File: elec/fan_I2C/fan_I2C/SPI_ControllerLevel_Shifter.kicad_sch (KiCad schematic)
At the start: 32 parts, among them J301 RJ12_6P6C_HORZ, J302 0.100_2Pin, Q301 BSS138, Q302 BSS138, Q303 BSS138, Q304 BSS138

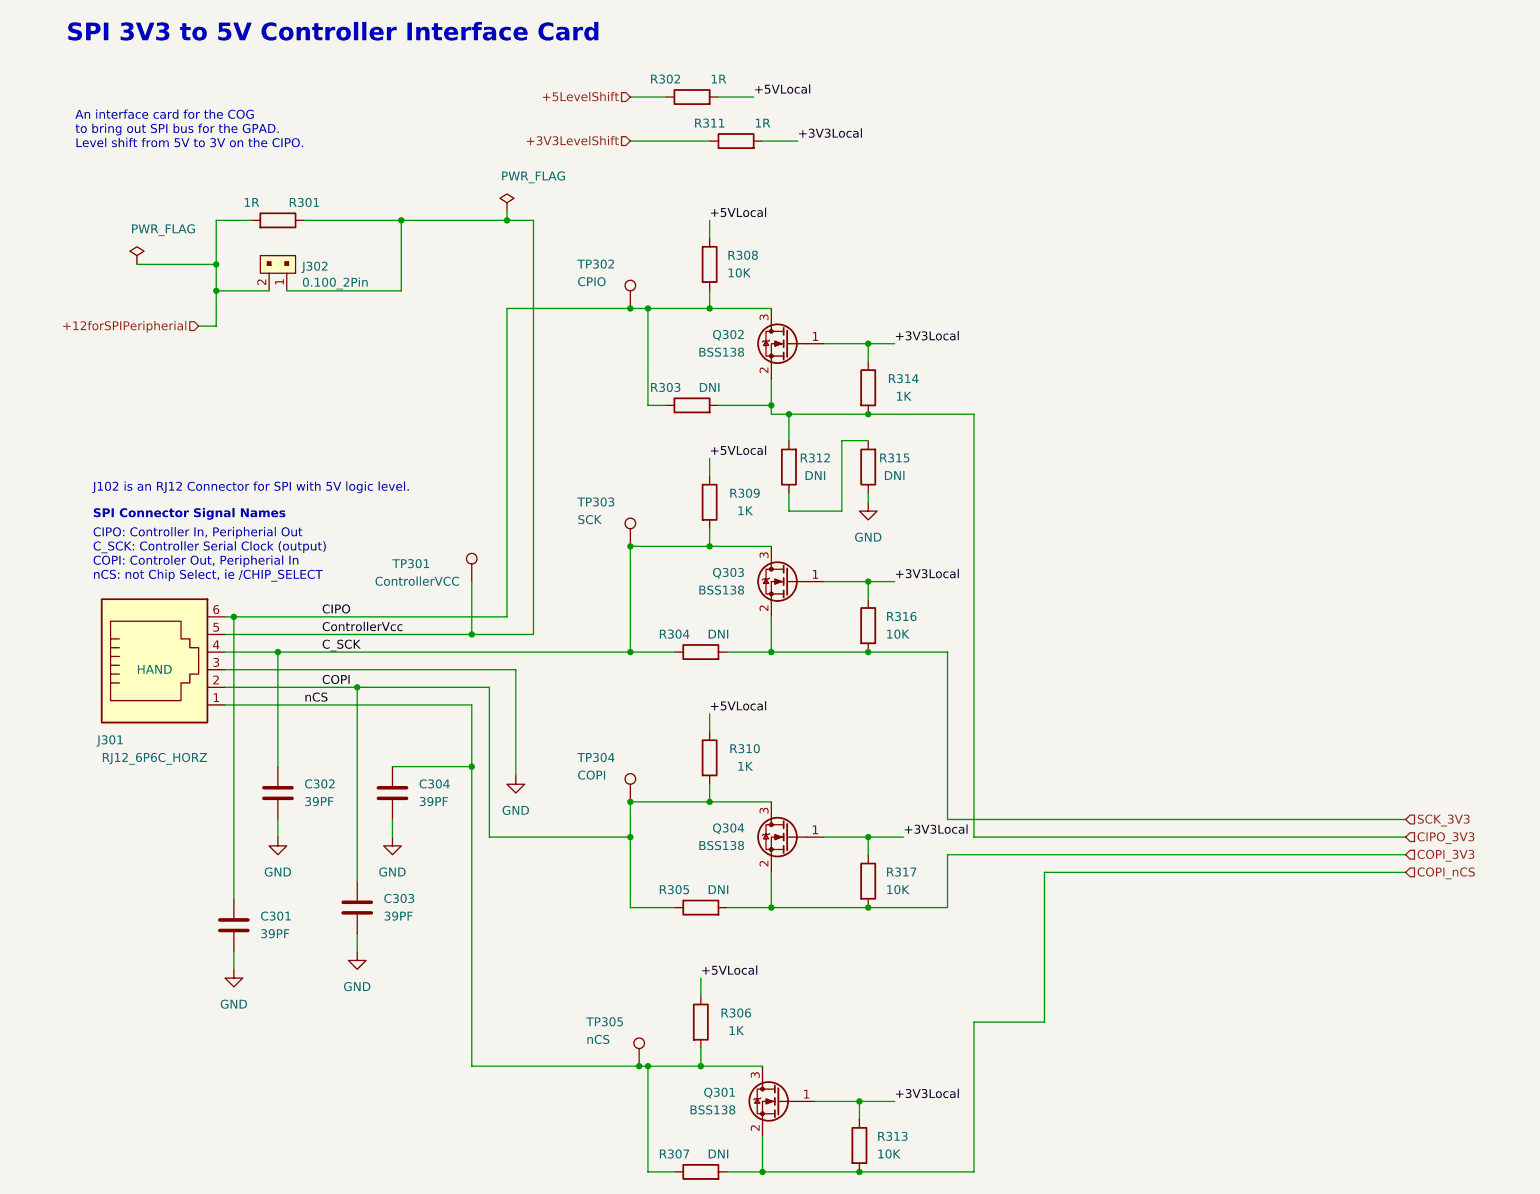
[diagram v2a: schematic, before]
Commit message: Add Connectors like Roberts Fritzing.
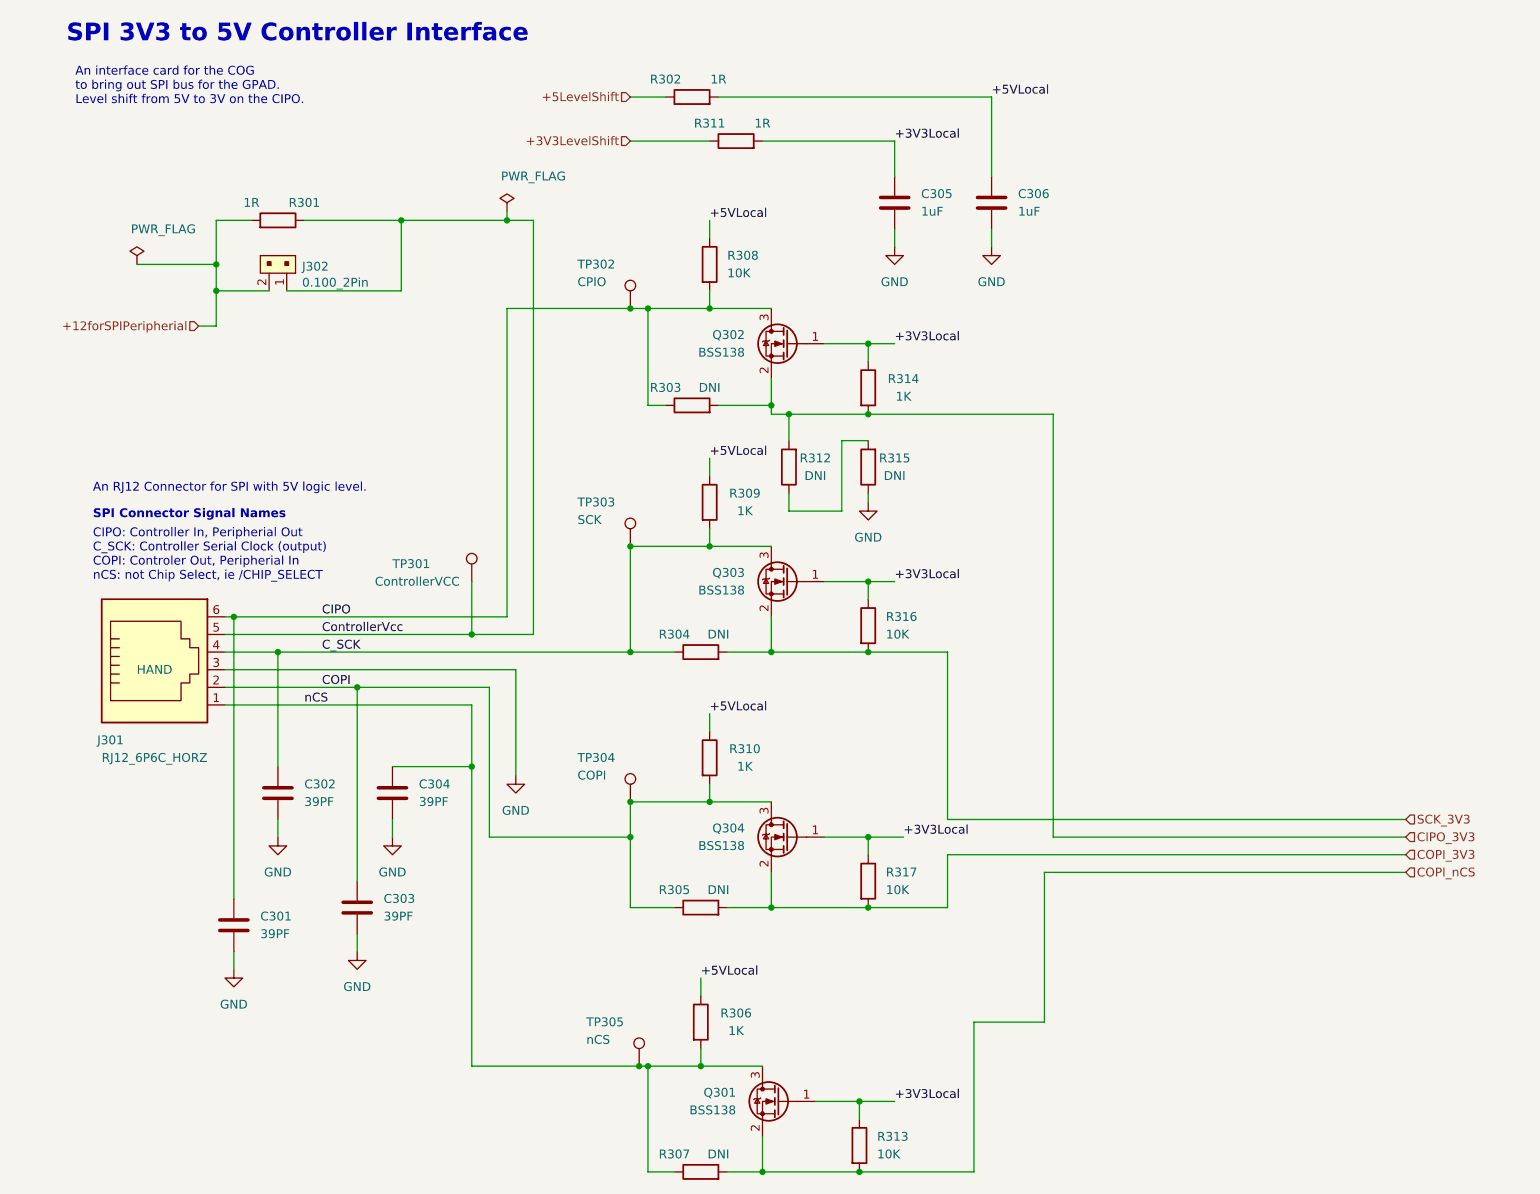
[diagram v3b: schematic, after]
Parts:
- added C305, C306: 1uF, Capacitor_SMD:C_0603_1608Metric_Pad1.08x0.95mm_HandSolder, symbol Device:C
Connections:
- net +3V3Local: now also C305.1
- net +5VLocal: now also C306.1
- net GND: now also C305.2, C306.2
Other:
- note added: "An RJ12 Connector for SPI with 5V logic level."
- note added: "SPI 3V3 to 5V Controller Interface"
- note removed: "J102 is an RJ12 Connector for SPI with 5V logic level."
- note removed: "SPI 3V3 to 5V Controller Interface Card"
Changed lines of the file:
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@@
+    (stroke (width 0) (type default) (color 0 0 0 0))
+  )
+  (wire (pts (xy 149.86 44.45) (xy 149.86 46.99))
     (stroke (width 0) (type default) (color 0 0 0 0))
   )
@@
     (stroke (width 0) (type default) (color 0 0 0 0))
   )
-  (wire (pts (xy 132.08 71.12) (xy 147.32 71.12))
+  (wire (pts (xy 132.08 71.12) (xy 158.75 71.12))
     (stroke (width 0) (type default) (color 0 0 0 0))
   )
@@
     (stroke (width 0) (type default) (color 0 0 0 0))
   )
+  (wire (pts (xy 135.89 44.45) (xy 135.89 46.99))
+    (stroke (width 0) (type default) (color 0 0 0 0))
+  )
   (wire (pts (xy 109.22 127) (xy 118.11 127))
     (stroke (width 0) (type default) (color 0 0 0 0))
@@
     (stroke (width 0) (type default) (color 0 0 0 0))
   )
-  (wire (pts (xy 147.32 132.08) (xy 147.32 71.12))
+  (wire (pts (xy 158.75 132.08) (xy 158.75 71.12))
     (stroke (width 0) (type default) (color 0 0 0 0))
   )
@@
     (stroke (width 0) (type default) (color 0 0 0 0))
   )
-  (wire (pts (xy 116.84 31.75) (xy 121.92 31.75))
+  (wire (pts (xy 116.84 31.75) (xy 135.89 31.75))
     (stroke (width 0) (type default) (color 0 0 0 0))
   )
@@
     (stroke (width 0) (type default) (color 0 0 0 0))
   )
-  (wire (pts (xy 110.49 25.4) (xy 115.57 25.4))
+  (wire (pts (xy 110.49 25.4) (xy 149.86 25.4))
     (stroke (width 0) (type default) (color 0 0 0 0))
   )
@@
     (stroke (width 0) (type default) (color 0 0 0 0))
   )
-  (wire (pts (xy 147.32 132.08) (xy 209.55 132.08))
+  (wire (pts (xy 158.75 132.08) (xy 209.55 132.08))
     (stroke (width 0) (type default) (color 0 0 0 0))
   )
@@
     (stroke (width 0) (type default) (color 0 0 0 0))
   )
+  (wire (pts (xy 149.86 25.4) (xy 149.86 36.83))
+    (stroke (width 0) (type default) (color 0 0 0 0))
+  )
   (wire (pts (xy 118.11 71.12) (xy 120.65 71.12))
     (stroke (width 0) (type default) (color 0 0 0 0))
@@
   )
   (wire (pts (xy 132.08 132.08) (xy 125.73 132.08))
+    (stroke (width 0) (type default) (color 0 0 0 0))
+  )
+  (wire (pts (xy 135.89 31.75) (xy 135.89 36.83))
     (stroke (width 0) (type default) (color 0 0 0 0))
   )
@@
     (effects (font (size 1.27 1.27) (thickness 0.254) bold) (justify left bottom))
   )
-  (text "SPI 3V3 to 5V Controller Interface Card\n" (at 16.51 17.78 0)
+  (text "SPI 3V3 to 5V Controller Interface\n" (at 16.51 17.78 0)
     (effects (font (size 2.54 2.54) (thickness 0.508) bold) (justify left bottom))
   )
@@
     (effects (font (size 1.27 1.27)) (justify left bottom))
   )
-  (text "J102 is an RJ12 Connector for SPI with 5V logic level."
-    (at 20.32 82.55 0)
+  (text "An RJ12 Connector for SPI with 5V logic level." (at 20.32 82.55 0)
     (effects (font (size 1.27 1.27)) (justify left bottom))
   )
   (text "An interface card for the COG\nto bring out SPI bus for the GPAD.  \nLevel shift from 5V to 3V on the CIPO.\n"
-    (at 17.78 33.02 0)
+    (at 17.78 26.67 0)
     (effects (font (size 1.27 1.27)) (justify left bottom))
   )
@@
     (effects (font (size 1.27 1.27)) (justify left bottom))
   )
-  (label "+3V3Local" (at 121.92 31.75 0)
+  (label "+3V3Local" (at 135.89 31.75 0)
     (effects (font (size 1.27 1.27)) (justify left bottom))
   )
@@
     (effects (font (size 1.27 1.27)) (justify left bottom))
   )
-  (label "+5VLocal" (at 115.57 25.4 0)
+  (label "+5VLocal" (at 149.86 25.4 0)
     (effects (font (size 1.27 1.27)) (justify left bottom))
   )
@@
     (pin "6")
   )
+  (symbol (lib_id "power:GND") (at 149.86 46.99 0) (unit 1)
+    (in_bom yes) (on_board yes) (fields_autoplaced)
+    (property "Reference" "#PWR0308" (id 0) (at 149.86 53.34 0)
+      (effects (font (size 1.27 1.27)) hide)
+    )
+    (property "Value" "GND" (id 1) (at 149.86 52.07 0))
+    (property "Footprint" "" (id 2) (at 149.86 46.99 0)
+      (effects (font (size 1.27 1.27)) hide)
+    )
+    (property "Datasheet" "" (id 3) (at 149.86 46.99 0)
+      (effects (font (size 1.27 1.27)) hide)
+    )
+    (pin "1")
+  )
   (symbol (lib_id "Device:R") (at 109.22 49.53 0) (unit 1)
     (in_bom yes) (on_board yes) (fields_autoplaced)
@@
   (symbol (lib_id "power:GND") (at 81.28 123.19 0) (unit 1)
     (in_bom yes) (on_board yes) (fields_autoplaced)
-    (property "Reference" "#PWR0109" (id 0) (at 81.28 129.54 0)
+    (property "Reference" "#PWR0305" (id 0) (at 81.28 129.54 0)
       (effects (font (size 1.27 1.27)) hide)
     )
@@
   (symbol (lib_id "power:GND") (at 132.08 83.82 0) (unit 1)
     (in_bom yes) (on_board yes) (fields_autoplaced)
-    (property "Reference" "#PWR0305" (id 0) (at 132.08 90.17 0)
+    (property "Reference" "#PWR0306" (id 0) (at 132.08 90.17 0)
       (effects (font (size 1.27 1.27)) hide)
     )
@@
     )
     (property "Datasheet" "" (id 3) (at 132.08 83.82 0)
+      (effects (font (size 1.27 1.27)) hide)
+    )
+    (pin "1")
+  )
+  (symbol (lib_id "power:GND") (at 135.89 46.99 0) (unit 1)
+    (in_bom yes) (on_board yes) (fields_autoplaced)
+    (property "Reference" "#PWR0307" (id 0) (at 135.89 53.34 0)
+      (effects (font (size 1.27 1.27)) hide)
+    )
+    (property "Value" "GND" (id 1) (at 135.89 52.07 0))
+    (property "Footprint" "" (id 2) (at 135.89 46.99 0)
+      (effects (font (size 1.27 1.27)) hide)
+    )
+    (property "Datasheet" "" (id 3) (at 135.89 46.99 0)
       (effects (font (size 1.27 1.27)) hide)
     )
@@
       (effects (font (size 1.27 1.27)) hide)
     )
+    (pin "1")
+    (pin "2")
+  )
+  (symbol (lib_id "Device:C") (at 135.89 40.64 0) (unit 1)
+    (in_bom yes) (on_board yes) (fields_autoplaced)
+    (property "Reference" "C305" (id 0) (at 139.7 39.3699 0)
+      (effects (font (size 1.27 1.27)) (justify left))
+    )
+    (property "Value" "1uF" (id 1) (at 139.7 41.9099 0)
+      (effects (font (size 1.27 1.27)) (justify left))
+    )
+    (property "Footprint" "Capacitor_SMD:C_0603_1608Metric_Pad1.08x0.95mm_HandSolder" (id 2) (at 136.8552 44.45 0)
+      (effects (font (size 1.27 1.27)) hide)
+    )
+    (property "Datasheet" "https://datasheet.lcsc.com/lcsc/1811082118_YAGEO-CC0603JRNPO9BN390_C107049.pdf" (id 3) (at 135.89 40.64 0)
+      (effects (font (size 1.27 1.27)) hide)
+    )
+    (property "AssemblyType" "SMT" (id 4) (at 135.89 40.64 0)
+      (effects (font (size 1.27 1.27)) hide)
+    )
+    (property "Distributor 1" "JLCPCB" (id 5) (at 135.89 40.64 0)
+      (effects (font (size 1.27 1.27)) hide)
+    )
+    (property "Distributor 1 PN" "" (id 6) (at 135.89 40.64 0)
+      (effects (font (size 1.27 1.27)) hide)
+    )
+    (property "Cost" "0.0025" (id 7) (at 135.89 40.64 0)
+      (effects (font (size 1.27 1.27)) hide)
+    )
+    (property "MPN" "" (id 8) (at 135.89 40.64 0)
+      (effects (font (size 1.27 1.27)) hide)
+    )
+    (property "Manufacturer" "YAGEO" (id 9) (at 135.89 40.64 0)
+      (effects (font (size 1.27 1.27)) hide)
+    )
+    (property "LongLead" "NO" (id 10) (at 135.89 40.64 0)
+      (effects (font (size 1.27 1.27)) hide)
+    )
+    (property "Description" "50V 1uF ±5% 0603 Multilayer Ceramic Ca" (id 11) (at 135.89 40.64 0)
+      (effects (font (size 1.27 1.27)) hide)
+    )
+    (pin "1")
+    (pin "2")
+  )
+  (symbol (lib_id "Device:C") (at 149.86 40.64 0) (unit 1)
+    (in_bom yes) (on_board yes) (fields_autoplaced)
+    (property "Reference" "C306" (id 0) (at 153.67 39.3699 0)
+      (effects (font (size 1.27 1.27)) (justify left))
+    )
+    (property "Value" "1uF" (id 1) (at 153.67 41.9099 0)
+      (effects (font (size 1.27 1.27)) (justify left))
+    )
+    (property "Footprint" "Capacitor_SMD:C_0603_1608Metric_Pad1.08x0.95mm_HandSolder" (id 2) (at 150.8252 44.45 0)
+      (effects (font (size 1.27 1.27)) hide)
+    )
+    (property "Datasheet" "https://datasheet.lcsc.com/lcsc/1811082118_YAGEO-CC0603JRNPO9BN390_C107049.pdf" (id 3) (at 149.86 40.64 0)
+      (effects (font (size 1.27 1.27)) hide)
+    )
+    (property "AssemblyType" "SMT" (id 4) (at 149.86 40.64 0)
+      (effects (font (size 1.27 1.27)) hide)
+    )
+    (property "Distributor 1" "JLCPCB" (id 5) (at 149.86 40.64 0)
+      (effects (font (size 1.27 1.27)) hide)
+    )
+    (property "Distributor 1 PN" "" (id 6) (at 149.86 40.64 0)
+      (effects (font (size 1.27 1.27)) hide)
+    )
+    (property "Cost" "0.0025" (id 7) (at 149.86 40.64 0)
+      (effects (font (size 1.27 1.27)) hide)
+    )
+    (property "MPN" "" (id 8) (at 149.86 40.64 0)
+      (effects (font (size 1.27 1.27)) hide)
+    )
+    (property "Manufacturer" "YAGEO" (id 9) (at 149.86 40.64 0)
+      (effects (font (size 1.27 1.27)) hide)
+    )
+    (property "LongLead" "NO" (id 10) (at 149.86 40.64 0)
+      (effects (font (size 1.27 1.27)) hide)
+    )
+    (property "Description" "50V 1uF ±5% 0603 Multilayer Ceramic Ca" (id 11) (at 149.86 40.64 0)
+      (effects (font (size 1.27 1.27)) hide)
+    )
